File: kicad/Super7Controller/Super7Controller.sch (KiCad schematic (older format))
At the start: 20 parts, among them P3 CONN_01X13, P4 CONN_01X09, U1 ULN2003A, U2 HiLetgo_ESP-WROOM-32_Developm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

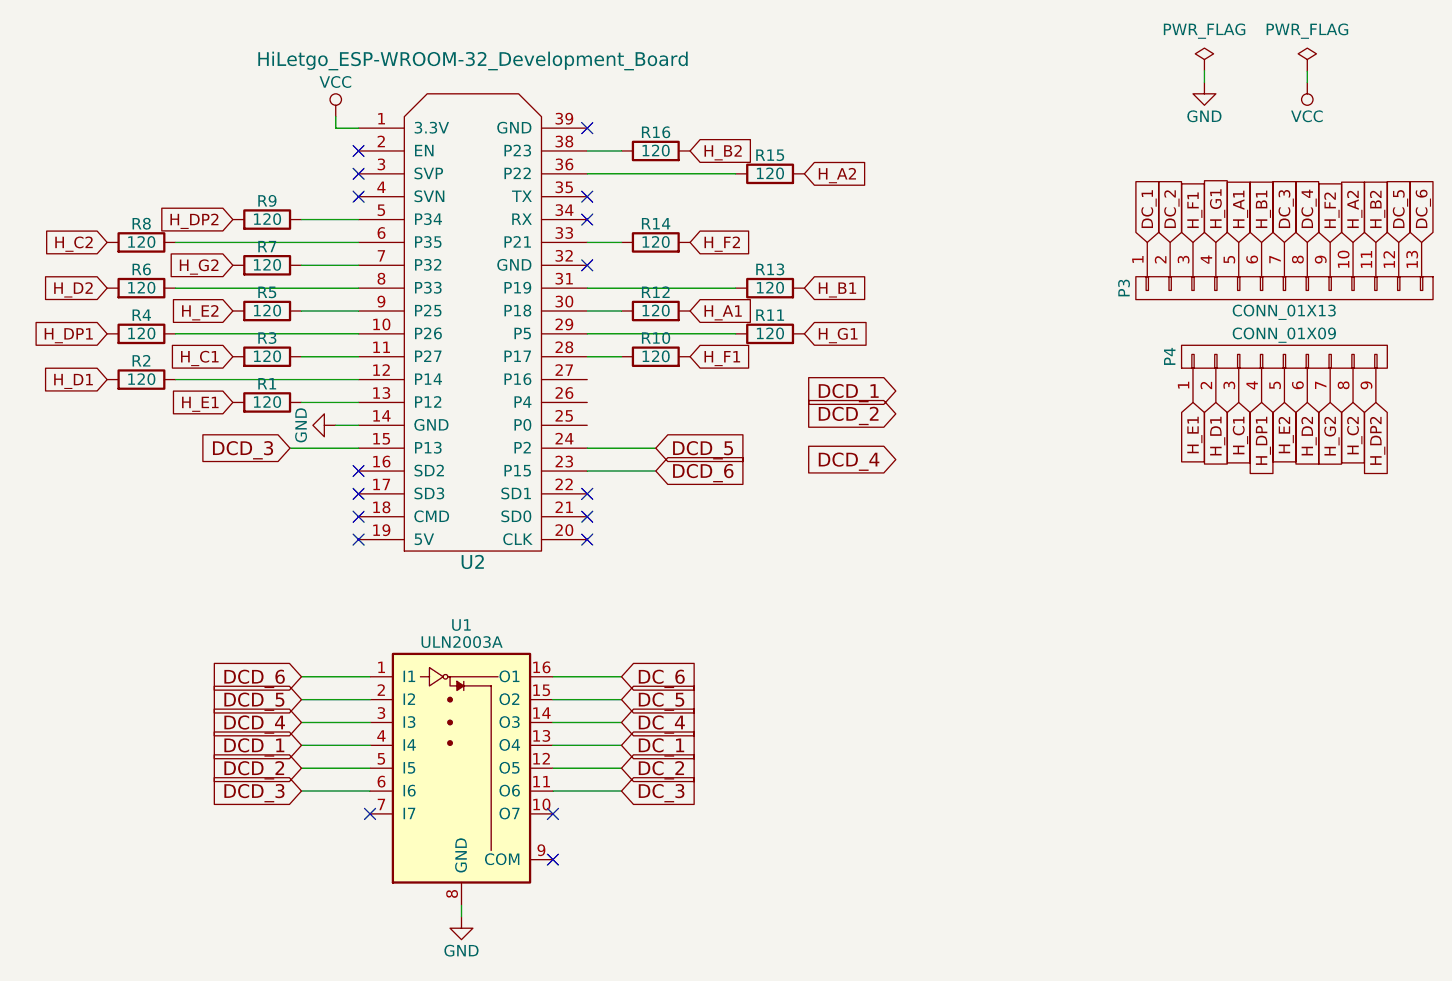
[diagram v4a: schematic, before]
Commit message: move ULN connections to make routing easier
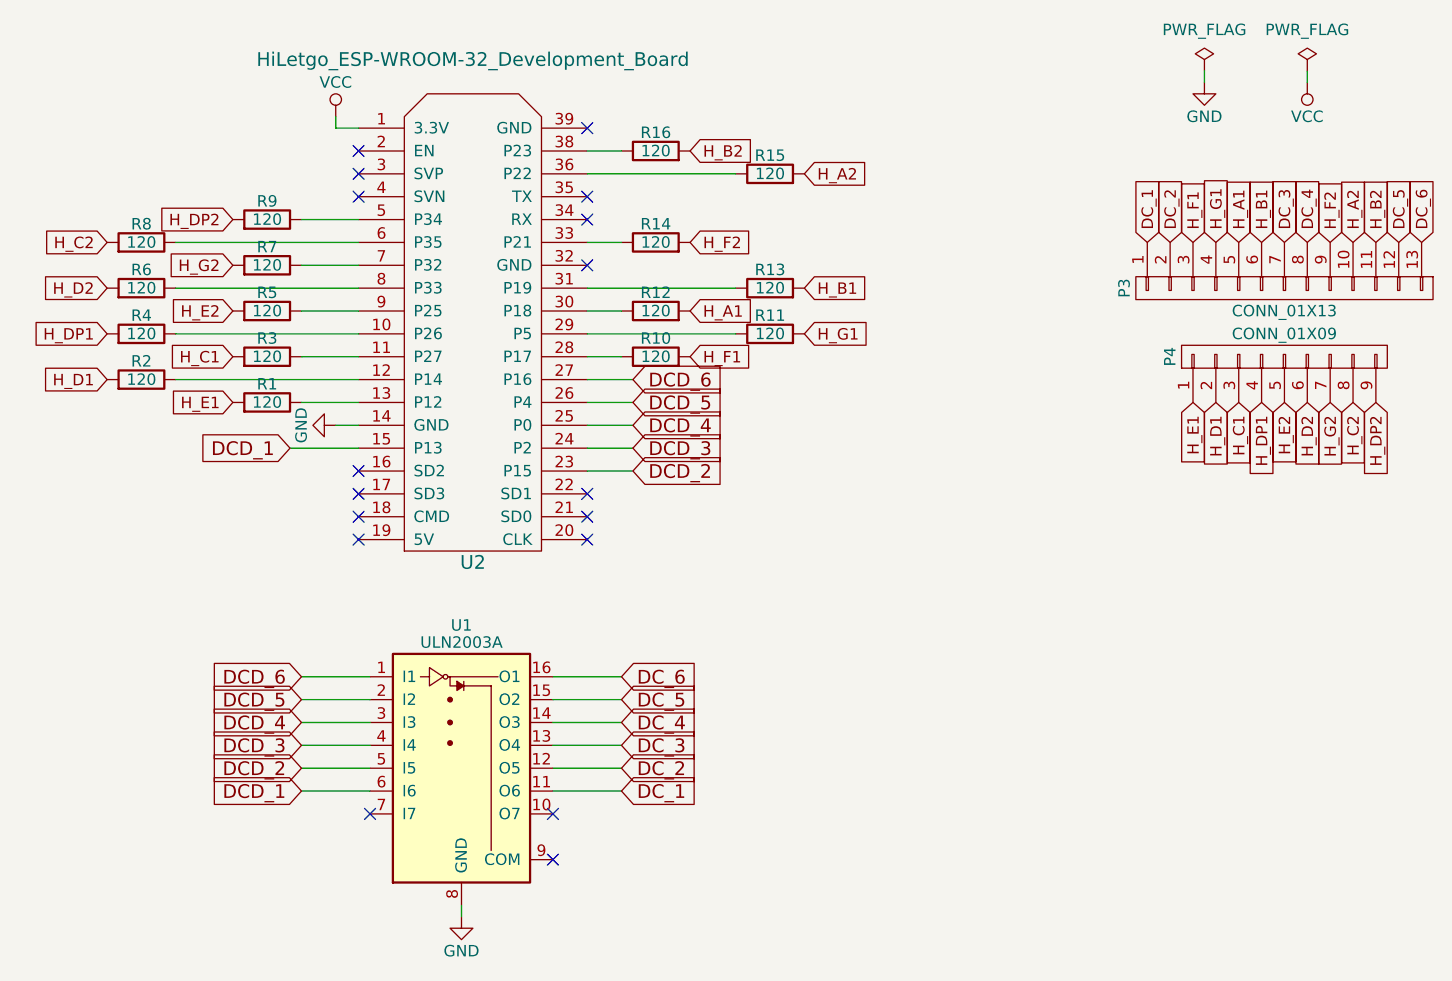
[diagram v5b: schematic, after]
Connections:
- net DCD_1: now also U1.6 (I6), U2.15 (P13); no longer U1.4 (I4)
- net DCD_2: now also U2.23 (P15)
- net DCD_3: now also U1.4 (I4), U2.24 (P2); no longer U1.6 (I6), U2.15 (P13)
- net DCD_4: now also U2.25 (P0)
- net DCD_5: now also U2.26 (P4); no longer U2.24 (P2)
- net DCD_6: now also U2.27 (P16); no longer U2.23 (P15)
- net DC_1: now also U1.11 (O6); no longer U1.13 (O4)
- net DC_3: now also U1.13 (O4); no longer U1.11 (O6)
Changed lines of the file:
@@
 	0    -1   -1   0
 $EndComp
-Text GLabel 7950 4350 2    60   Input ~ 0
+Text GLabel 7950 4550 2    60   Input ~ 0
 DC_1
 Text GLabel 7950 4450 2    60   Input ~ 0
 DC_2
-Text GLabel 7950 4550 2    60   Input ~ 0
+Text GLabel 7950 4350 2    60   Input ~ 0
 DC_3
 Text GLabel 7950 4250 2    60   Input ~ 0
@@
 NoConn ~ 7800 2250
 NoConn ~ 7800 1650
-Text GLabel 6550 4350 0    60   Input ~ 0
+Text GLabel 6550 4550 0    60   Input ~ 0
 DCD_1
 Text GLabel 6550 4450 0    60   Input ~ 0
 DCD_2
-Text GLabel 6550 4550 0    60   Input ~ 0
+Text GLabel 6550 4350 0    60   Input ~ 0
 DCD_3
 Text GLabel 6550 4250 0    60   Input ~ 0
@@
 DCD_6
 Wire Wire Line
-	7950 4350 7650 4350
-Wire Wire Line
 	7650 4450 7950 4450
-Wire Wire Line
-	7650 4550 7950 4550
 Wire Wire Line
 	7650 4250 7950 4250
@@
 	6850 4250 6550 4250
 Wire Wire Line
-	6550 4350 6850 4350
-Wire Wire Line
 	6850 4450 6550 4450
-Wire Wire Line
-	6550 4550 6850 4550
-Text GLabel 8100 3150 2    60   Input ~ 0
+Text GLabel 8000 2750 2    60   Input ~ 0
 DCD_6
-Wire Wire Line
-	7800 3150 8100 3150
-Text GLabel 8100 3050 2    60   Input ~ 0
+Text GLabel 8000 2850 2    60   Input ~ 0
 DCD_5
-Wire Wire Line
-	7800 3050 8100 3050
+Text GLabel 8000 3050 2    60   Input ~ 0
+DCD_3
+Text GLabel 8000 3150 2    60   Input ~ 0
+DCD_2
 Text GLabel 6500 3050 0    60   Input ~ 0
-DCD_3
-Wire Wire Line
-	6800 3050 6500 3050
-Text GLabel 9150 2900 0    60   Input ~ 0
-DCD_2
-Text GLabel 9150 2800 0    60   Input ~ 0
 DCD_1
-Text GLabel 9150 3100 0    60   Input ~ 0
+Text GLabel 8000 2950 2    60   Input ~ 0
 DCD_4
 Wire Wire Line
@@
 Wire Wire Line
 	7800 2650 7950 2650
+Wire Wire Line
+	6850 4350 6550 4350
+Wire Wire Line
+	6550 4550 6850 4550
+Wire Wire Line
+	7650 4550 7950 4550
+Wire Wire Line
+	7950 4350 7650 4350
+Wire Wire Line
+	6800 3050 6500 3050
+Wire Wire Line
+	8000 2750 7800 2750
+Wire Wire Line
+	7800 2850 8000 2850
+Wire Wire Line
+	8000 2950 7800 2950
+Wire Wire Line
+	7800 3050 8000 3050
+Wire Wire Line
+	8000 3150 7800 3150
 $EndSCHEMATC

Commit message: 2 to 6 is better
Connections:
- net DCD_2: now also U2.27 (P16); no longer U2.23 (P15)
- net DCD_3: now also U2.26 (P4); no longer U2.24 (P2)
- net DCD_5: now also U2.24 (P2); no longer U2.26 (P4)
- net DCD_6: now also U2.23 (P15); no longer U2.27 (P16)
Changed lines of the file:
@@
 Wire Wire Line
 	6850 4450 6550 4450
+Text GLabel 8000 3150 2    60   Input ~ 0
+DCD_6
+Text GLabel 8000 3050 2    60   Input ~ 0
+DCD_5
+Text GLabel 8000 2850 2    60   Input ~ 0
+DCD_3
 Text GLabel 8000 2750 2    60   Input ~ 0
-DCD_6
-Text GLabel 8000 2850 2    60   Input ~ 0
-DCD_5
-Text GLabel 8000 3050 2    60   Input ~ 0
-DCD_3
-Text GLabel 8000 3150 2    60   Input ~ 0
 DCD_2
 Text GLabel 6500 3050 0    60   Input ~ 0
@@
 	6800 3050 6500 3050
 Wire Wire Line
-	8000 2750 7800 2750
+	7800 2750 8000 2750
 Wire Wire Line
-	7800 2850 8000 2850
+	8000 2850 7800 2850
 Wire Wire Line
-	8000 2950 7800 2950
+	7800 2950 8000 2950
 Wire Wire Line
-	7800 3050 8000 3050
+	8000 3050 7800 3050
 Wire Wire Line
-	8000 3150 7800 3150
+	7800 3150 8000 3150
 $EndSCHEMATC

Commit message: use new KiCad header instead of old one
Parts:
- removed P3: CONN_01X13, Socket_Strips:Socket_Strip_Straight_1x13, symbol CONN_01X13
- removed P4: CONN_01X09, Socket_Strips:Socket_Strip_Straight_1x09, symbol CONN_01X09
- added P3: Conn_01x13, symbol Conn_01x13
- added P4: Conn_01x09, symbol Conn_01x09
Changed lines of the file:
@@
 Text GLabel 11350 2150 1    50   Input ~ 0
 DC_5
-$Comp
-L CONN_01X13 P3
-U 1 1 5867A2A3
-P 10850 2350
-F 0 "P3" H 10850 3050 50  0000 C CNN
-F 1 "CONN_01X13" V 10950 2350 50  0000 C CNN
-F 2 "Socket_Strips:Socket_Strip_Straight_1x13" H 10850 2350 50  0001 C CNN
-F 3 "" H 10850 2350 50  0000 C CNN
-	1    10850 2350
-	0    -1   1    0
-$EndComp
-$Comp
-L CONN_01X09 P4
-U 1 1 5867A59F
-P 10850 2650
-F 0 "P4" H 10850 3150 50  0000 C CNN
-F 1 "CONN_01X09" V 10950 2650 50  0000 C CNN
-F 2 "Socket_Strips:Socket_Strip_Straight_1x09" H 10850 2650 50  0001 C CNN
-F 3 "" H 10850 2650 50  0000 C CNN
-	1    10850 2650
-	0    -1   -1   0
-$EndComp
 Text GLabel 7950 4550 2    60   Input ~ 0
 DC_1
@@
 Wire Wire Line
 	7800 3150 8000 3150
+$Comp
+L Conn_01x13 P3
+U 1 1 5A7CB928
+P 10850 2350
+F 0 "P3" H 10850 3050 50  0000 C CNN
+F 1 "Conn_01x13" H 10850 1650 50  0000 C CNN
+F 2 "" H 10850 2350 50  0001 C CNN
+F 3 "" H 10850 2350 50  0001 C CNN
+	1    10850 2350
+	0    -1   1    0
+$EndComp
+$Comp
+L Conn_01x09 P4
+U 1 1 5A7CBA4E
+P 10850 2650
+F 0 "P4" H 10850 3150 50  0000 C CNN
+F 1 "Conn_01x09" H 10850 2150 50  0000 C CNN
+F 2 "" H 10850 2650 50  0001 C CNN
+F 3 "" H 10850 2650 50  0001 C CNN
+	1    10850 2650
+	0    -1   -1   0
+$EndComp
 $EndSCHEMATC

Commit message: new footprint for headers
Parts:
- P3: footprint (none) -> Socket_Strips:Socket_Strip_Straight_1x13_Pitch2.54mm
- P4: footprint (none) -> Socket_Strips:Socket_Strip_Straight_1x09_Pitch2.54mm
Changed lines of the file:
@@
 F 0 "P3" H 10850 3050 50  0000 C CNN
 F 1 "Conn_01x13" H 10850 1650 50  0000 C CNN
-F 2 "" H 10850 2350 50  0001 C CNN
+F 2 "Socket_Strips:Socket_Strip_Straight_1x13_Pitch2.54mm" H 10850 2350 50  0001 C CNN
 F 3 "" H 10850 2350 50  0001 C CNN
 	1    10850 2350
@@
 F 0 "P4" H 10850 3150 50  0000 C CNN
 F 1 "Conn_01x09" H 10850 2150 50  0000 C CNN
-F 2 "" H 10850 2650 50  0001 C CNN
+F 2 "Socket_Strips:Socket_Strip_Straight_1x09_Pitch2.54mm" H 10850 2650 50  0001 C CNN
 F 3 "" H 10850 2650 50  0001 C CNN
 	1    10850 2650
